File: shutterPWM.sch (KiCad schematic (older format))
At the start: 22 parts, among them P10 2x3 header strip R/A, P11 2x3 header strip R/A, U1 DRV103, U2 DRV103

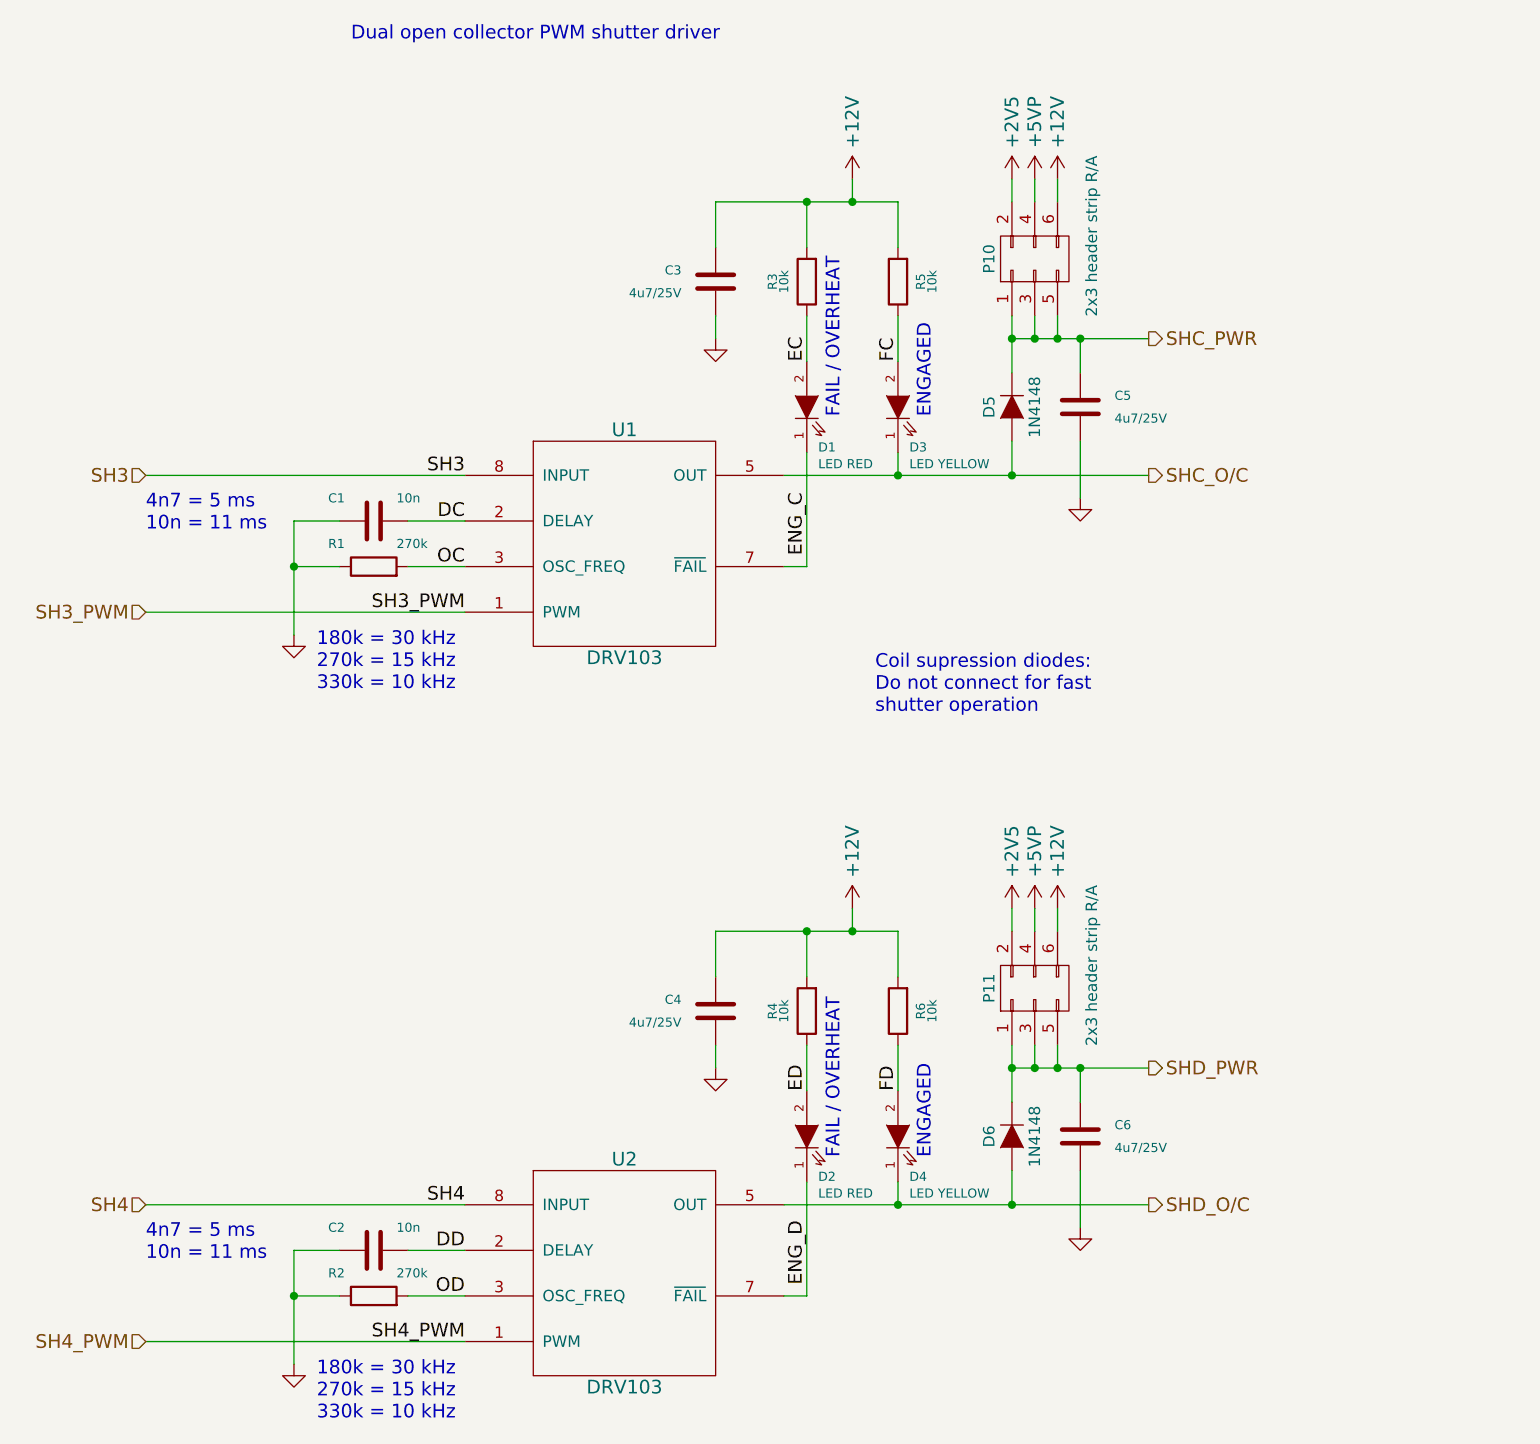
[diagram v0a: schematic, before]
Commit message: Added better de-bouncing diode description
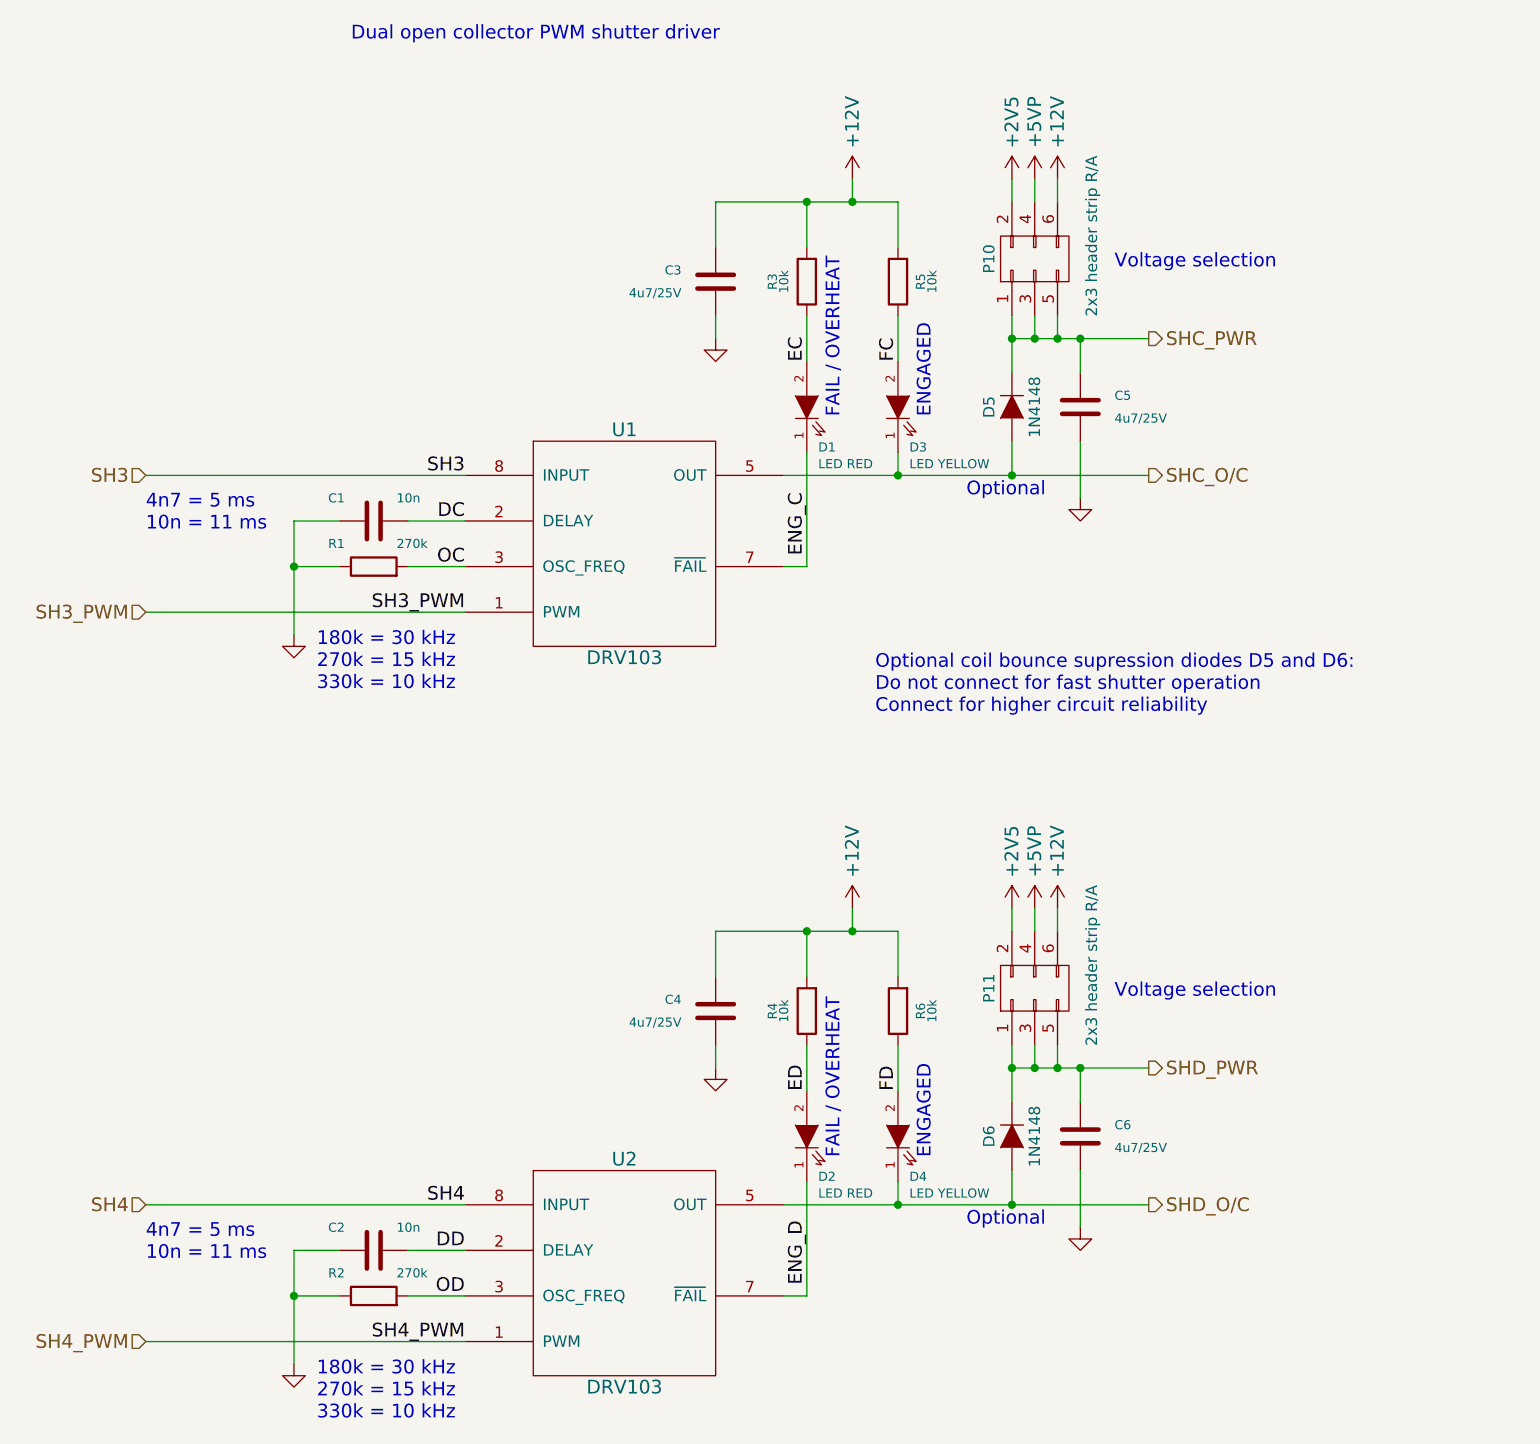
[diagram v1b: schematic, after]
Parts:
- D5, D6: Note Small signal SOD-323 diode -> Optional small signal SOD-323 diode
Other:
- note added: "Optional"
- note added: "Optional coil bounce supression diodes D5 and D6:\nDo not connect for fast shutter operation\nConnect for higher circuit reliability"
- note added: "Voltage selection"
- note removed: "Coil supression diodes:\nDo not connect for fast\nshutter operation"
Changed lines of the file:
@@
 $EndComp
 Text Notes 4500 3650 0    60   ~ 0
-Coil supression diodes:\nDo not connect for fast\nshutter operation
+Optional coil bounce supression diodes D5 and D6:\nDo not connect for fast shutter operation\nConnect for higher circuit reliability
 $Comp
 L C C3
@@
 F 9 "Mouser" H 5100 2300 60  0001 C CNN "Alt. Supplier"
 F 10 "512-1N4148WS" H 5100 2300 60  0001 C CNN "Alt. Order Code"
-F 11 "Small signal SOD-323 diode" H 5100 2300 60  0001 C CNN "Note"
+F 11 "Optional small signal SOD-323 diode" H 5100 2300 60  0001 C CNN "Note"
 	1    5100 2300
 	0    1    1    0
@@
 F 9 "Mouser" H 5100 5500 60  0001 C CNN "Alt. Supplier"
 F 10 "512-1N4148WS" H 5100 5500 60  0001 C CNN "Alt. Order Code"
-F 11 "Small signal SOD-323 diode" H 5100 5500 60  0001 C CNN "Note"
+F 11 "Optional small signal SOD-323 diode" H 5100 5500 60  0001 C CNN "Note"
 	1    5100 5500
 	0    1    1    0
 $EndComp
+Text Notes 5550 1700 0    60   ~ 0
+Voltage selection
+Text Notes 5550 4900 0    60   ~ 0
+Voltage selection
+Text Notes 4900 2700 0    60   ~ 0
+Optional
+Text Notes 4900 5900 0    60   ~ 0
+Optional
 $EndSCHEMATC

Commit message: Changed ENGAGED LED anode to +5V, changed SOD-323 packages, tidied up layout
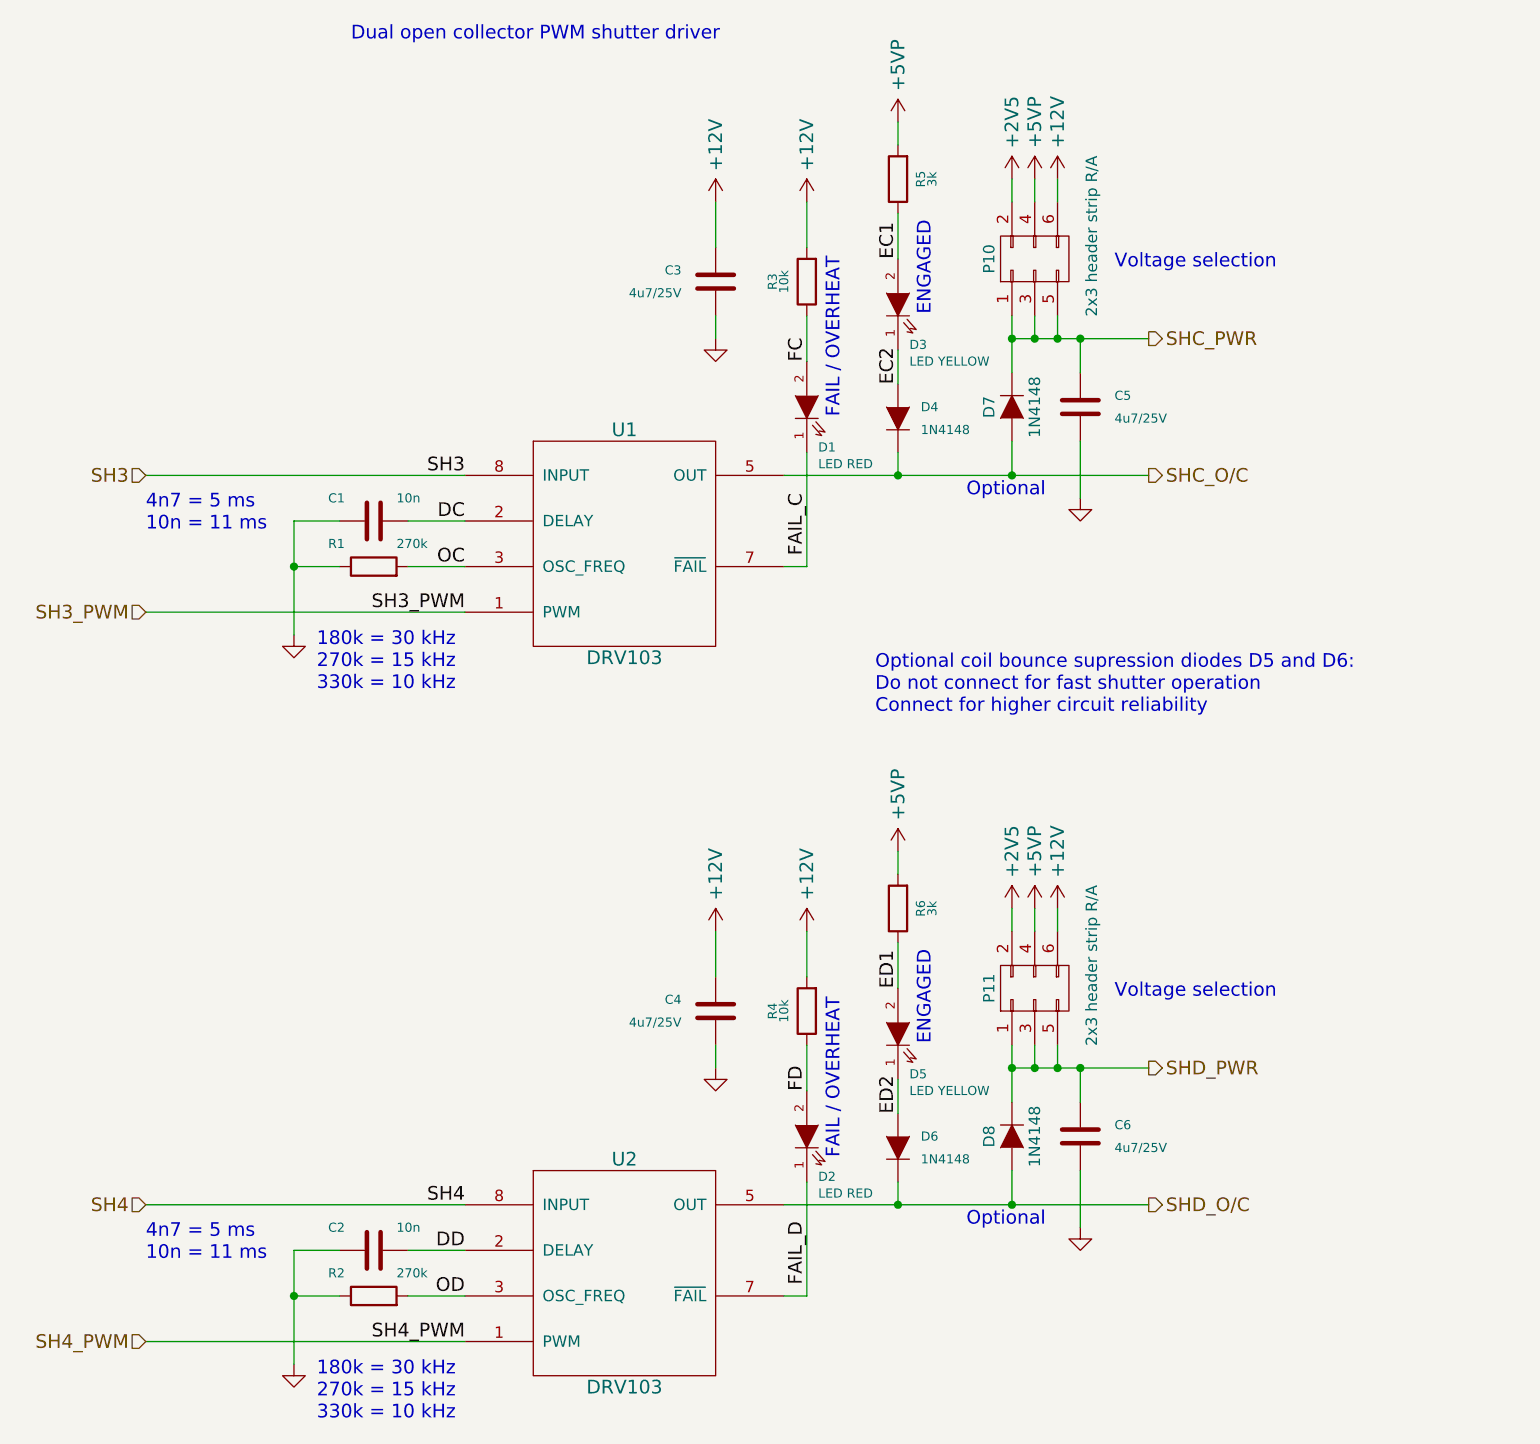
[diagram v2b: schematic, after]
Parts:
- removed D4: LED YELLOW, LEDs:LED-1206, symbol LED
- added D5: LED YELLOW, LEDs:LED-1206, symbol LED
- added D6, D7: 1N4148, jakub:SOD-323, symbol D
- D1, D2: Manufacturer Lumex -> Broadcom
- D3: Manufacturer Avago -> Broadcom
- D4: renamed from D5; footprint Diodes_SMD:SOD-323 -> jakub:SOD-323
- D8: renamed from D6; footprint Diodes_SMD:SOD-323 -> jakub:SOD-323
- R5, R6: value 10k -> 3k; Alt. Order Code 71-CRCW0805-10K-E3 -> 667-ERJ-6GEYJ302V; Note 10kΩ/1% 0805 resistor -> 3kΩ/1% 0805 resistor; Order Code 2073607 -> 9332995; Part Number MCMR08X1002FTL -> MC01W080513K
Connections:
- net EC is gone; now on net FC: D1.2 (A), R3.1
- net ED is gone; now on net FD: D2.2 (A), R4.1
- net +12V: no longer R5.2, R6.2
- net +5VP: now also R5.2, R6.2
- net FC: no longer D3.2 (A), R5.1
- net FD: no longer R6.1
- net SHC_O/C: now also D4.1 (K), D7.2 (A); no longer D3.1 (K), D4.2 (A)
- net SHC_PWR: now also D7.1 (K); no longer D4.1 (K)
- net SHD_O/C: now also D6.1 (K)
- net ENG_C renamed FAIL_C
- net ENG_D renamed FAIL_D
- new net EC1: D3.2 (A), R5.1
- new net EC2: D3.1 (K), D4.2 (A)
- new net ED1: D5.2 (A), R6.1
- new net ED2: D5.1 (K), D6.2 (A)
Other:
- moved on the sheet: D3, D4
